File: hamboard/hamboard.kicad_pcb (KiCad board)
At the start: 2 copper layers, 83 parts, among them J1 Conn_01x03_Male, J3 USB_B_Micro, J4 Screw_Terminal_Btn, J5 Screw_Terminal_01x02, J6 programmer, J7 weight, J8 STEPPER, J9 Barrel_Jack, Q1 AO3400A, Q2 S8050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

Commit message: board: bom
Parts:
- added C33: 100nF, Capacitor_SMD:C_0805_2012Metric, F.Cu at (204.5, 92.7)
- added C34: 15pF, Capacitor_SMD:C_0805_2012Metric, F.Cu at (134.6, 90.2)
- added F1: Polyfuse 24V/4A, Fuse:Fuse_2920_7451Metric, F.Cu at (203.2, 111.6)
- added J1: i2c, TerminalBlock:TerminalBlock_bornier-4_P5.08mm, F.Cu at (177.6, 95.7)
- added J10: Conn_01x03_Male, Connector_PinHeader_2.54mm:PinHeader_1x03_P2.54mm_Vertical, F.Cu at (153.9, 82.0)
- added J2: Conn_01x24_Male, Connector_FFC-FPC:Hirose_FH12-24S-0.5SH_1x24-1MP_P0.50mm_Horizontal, F.Cu at (142.0, 83.2)
- added Q2: S8050, Package_TO_SOT_SMD:SOT-23, F.Cu at (176.8, 102.5)
- added Q3: S8050, Package_TO_SOT_SMD:SOT-23, F.Cu at (181.7, 102.5)
- added Q4: MMBT4403, Package_TO_SOT_SMD:SOT-23, F.Cu at (176.8, 110.3)
- added R3: 9k1, Resistor_SMD:R_0805_2012Metric, F.Cu at (134.6, 98.9)
- added R6: 1k, Resistor_SMD:R_0805_2012Metric, F.Cu at (139.1, 90.9)
- added TP10: TestPoint, TestPoint:TestPoint_Pad_D1.5mm, F.Cu at (146.6, 90.4)
- added TP11: TestPoint, TestPoint:TestPoint_Pad_D1.5mm, F.Cu at (143.0, 90.4)
- C10, C13, C14: value 10uF -> 1uF
- C11: value 10uF -> 100nF
- C12: value 10uF -> 10nF
- C19: value 100nF -> 1uF
- C21, C27, C8: value C -> 10nF
- C24, C6: value C -> 1uF
- C26, C7: value C -> 100nF
- C28: footprint Capacitor_SMD:CP_Elec_8x10 -> Capacitor_SMD:CP_Elec_6.3x7.7
- C3, C9: value 0.1uF -> 100nF
- C30: value 470uF/50V -> 680uF/50V; footprint Capacitor_SMD:CP_Elec_16x17.5 -> Capacitor_THT:CP_Radial_D13.0mm_P5.00mm
- C31: value C -> 100n
- C32: footprint Capacitor_SMD:CP_Elec_10x12.5 -> Capacitor_SMD:CP_Elec_10x10.5
- C4: value C -> 1uf
- C5: value ? -> 100nF
- D1, D2: footprint Diode_SMD:D_SOD-923 -> hamboard:Diodes_DFN1006
- D3: value SD24_SOD323 -> SD24_SOD523; footprint Diode_SMD:D_SOD-323 -> Diode_SMD:D_SOD-523
- D4: value D_Zener -> D_Zener 25V
- D5: footprint lib:DIOM6859X262N -> Diode_SMD:D_SMA
- J3: footprint Connector_USB:USB_Micro-B_Molex-105017-0001 -> Connector_USB:USB_Micro-B_GCT_USB3076-30-A
- J4, J5: footprint Connector_Phoenix_MSTB:PhoenixContact_MSTBA_2,5_2-G-5,08_1x02_P5.08mm_Horizontal -> TerminalBlock:TerminalBlock_bornier-2_P5.08mm
- J8: footprint Connector_Phoenix_MSTB:PhoenixContact_MSTBA_2,5_4-G-5,08_1x04_P5.08mm_Horizontal -> TerminalBlock:TerminalBlock_bornier-4_P5.08mm
- R1, R2, R9: value R -> 10k
- R11: value 0R -> 10k
- R19: value R -> 12k
- U3: footprint Package_SO:SOIC-16_3.9x9.9mm_P1.27mm -> Package_SO:SOP-16_3.9x9.9mm_P1.27mm
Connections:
- net Net-(C18-Pad1) renamed /Stepper_driver/5VOUT
- J4 pad 1: /BTN -> Net-(J4-Pad1)
- R12 pad 1: Net-(Q3-Pad1) -> Net-(R12-Pad1)
- R12 pad 2: Net-(Q2-Pad2) -> Net-(R12-Pad2)
- R13 pad 1: Net-(Q2-Pad1) -> Net-(R13-Pad1)
- R13 pad 2: Net-(Q3-Pad2) -> Net-(R13-Pad2)
- U1 pad 12: Net-(TP1-Pad1) -> Net-(U1-Pad12)
- U1 pad 13: Net-(TP2-Pad1) -> Net-(U1-Pad13)
- U1 pad 14: Net-(TP3-Pad1) -> Net-(U1-Pad14)
- U3 pad 13: Net-(Q3-Pad1) -> Net-(R12-Pad1)
- U3 pad 14: Net-(Q2-Pad1) -> Net-(R13-Pad1)
- U5 pad 23: unconnected-(U5-Pad23) -> Net-(R3-Pad2)
- U5 pad 37: unconnected-(U5-Pad37) -> GND
- U7 pad 4: unconnected-(U7-Pad4) -> GND

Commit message: first pcb layout
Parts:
- removed the J1 at (100.0, 89.1)
- removed the Q2 at (123.6, 72.4)
- removed the Q3 at (130.6, 69.4)
- removed TP1, TP2, TP3, TP6: TestPoint, TestPoint:TestPoint_Pad_D1.5mm
- C15: value 22n -> 22nF
- C17: value 470n -> 470nF
- C31: value 100n -> 100nF
- C4: value 1uf -> 1uF
- D4: footprint Capacitor_SMD:CP_Elec_8x10 -> Diode_SMD:D_MiniMELF
- D5: footprint Diode_SMD:D_SMA -> lib:DIOM6859X262N
- J1: footprint TerminalBlock:TerminalBlock_bornier-4_P5.08mm -> Connector_PinHeader_2.54mm:PinHeader_1x04_P2.54mm_Vertical
- J7: footprint Connector_Phoenix_MSTB:PhoenixContact_MSTBA_2,5_4-G-5,08_1x04_P5.08mm_Horizontal -> TerminalBlock:TerminalBlock_bornier-4_P5.08mm
- R14, R15, R16, R17: value 100R -> 100
- moved F1 176.3 mm to (39.3, 46.7)
- moved C33 170.5 mm to (34.0, 89.7), turned to -90 degrees
- moved C17 153.3 mm to (29.2, 86.6), turned to 180 degrees
- moved R18 152.7 mm to (29.2, 84.6)
- moved U5 149.4 mm to (35.1, 84.1), turned to 180 degrees
- moved Q3 142.9 mm to (38.9, 96.8)
- moved C18 139.5 mm to (29.2, 82.5)
- moved J8 138.5 mm to (21.3, 74.2), turned to -90 degrees
- moved Q2 137.9 mm to (38.9, 100.6)
- moved C20 136.2 mm to (36.8, 78.7), turned to 90 degrees
- moved C21 129.8 mm to (38.9, 78.7), turned to 90 degrees
- moved C28 129.7 mm to (30.7, 73.7), turned to 180 degrees
- moved C15 127.5 mm to (29.2, 88.9), turned to 180 degrees
- moved C16 124.9 mm to (32.0, 89.7), turned to -90 degrees
- moved TP10 123.2 mm to (23.9, 101.6)
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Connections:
- J10 pad 1: Net-(U1-Pad14) -> Net-(J10-Pad1)
- J10 pad 2: Net-(U1-Pad13) -> Net-(J10-Pad2)
- J10 pad 3: Net-(U1-Pad12) -> Net-(J10-Pad3)
- J5 pad 1: +24V -> Net-(J5-Pad1)
- J5 pad 2: Net-(J5-Pad2) -> +24V
- Q1 pad 3: Net-(J5-Pad2) -> Net-(J5-Pad1)
- U1 pad 10: /STEPPER_EN -> Net-(J10-Pad3)
- U1 pad 11: /STEPPER_DIR -> Net-(J10-Pad2)
- U1 pad 12: Net-(U1-Pad12) -> Net-(J10-Pad1)
- U1 pad 13: Net-(U1-Pad13) -> /STEPPER_EN
- U1 pad 14: Net-(U1-Pad14) -> /STEPPER_DIR
- U1 pad 6: /CAM_RST -> /CAM_PWN
- U1 pad 7: /CAM_PWN -> /CAM_RST
- U2 pad 10: /CAM_Y2 -> /CAM_Y7
- U2 pad 11: /CAM_Y5 -> /CAM_Y8
- U2 pad 12: /CAM_Y3 -> /CAM_XCLK
- U2 pad 13: /I2C_SDA -> /CAM_Y9
- U2 pad 14: /STEPPER_SCK -> /CAM_HREF
- U2 pad 16: /I2C_SCL -> /CAM_VSYNC
- U2 pad 23: /CAM_Y9 -> /I2C_SCL
- U2 pad 24: /CAM_HREF -> /I2C_SDA
- U2 pad 26: /STEPPER_SDI -> /STEPPER_STEP
- U2 pad 29: /CAM_VSYNC -> /STEPPER_SDO
- U2 pad 30: /CAM_XCLK -> /STEPPER_SDI
- U2 pad 31: /STEPPER_CS -> /STEPPER_SCK
- U2 pad 33: /STEPPER_STEP -> /STEPPER_CS
- U2 pad 36: /CAM_PCLK -> /BTN
- U2 pad 39_1: Net-(U2-Pad39_1) -> GND
- U2 pad 39_2: Net-(U2-Pad39_1) -> GND
- U2 pad 39_3: Net-(U2-Pad39_1) -> GND
- U2 pad 39_4: Net-(U2-Pad39_1) -> GND
- U2 pad 39_5: Net-(U2-Pad39_1) -> GND
- U2 pad 39_6: Net-(U2-Pad39_1) -> GND
- U2 pad 39_7: Net-(U2-Pad39_1) -> GND
- U2 pad 39_8: Net-(U2-Pad39_1) -> GND
- U2 pad 39_9: Net-(U2-Pad39_1) -> GND
- U2 pad 4: /CAM_Y7 -> /CAM_Y4
- U2 pad 5: /CAM_Y6 -> /CAM_Y3
- U2 pad 6: /BTN -> /CAM_Y5
- U2 pad 7: /CAM_Y8 -> /CAM_Y2
- U2 pad 8: /CAM_Y4 -> /CAM_Y6
- U2 pad 9: /STEPPER_SDO -> /CAM_PCLK
- U5 pad 13: Net-(J8-Pad3) -> Net-(J8-Pad2)
- U5 pad 15: Net-(J8-Pad4) -> Net-(J8-Pad1)
- U5 pad 32: Net-(J8-Pad2) -> Net-(J8-Pad3)
- U5 pad 34: Net-(J8-Pad1) -> Net-(J8-Pad4)
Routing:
- net +3V3: track 0.00 -> 258.0 mm, vias 0 -> 2
- net +24V: track 0.00 -> 118.6 mm
- net /IO0: track 0.00 -> 81.4 mm, vias 0 -> 3
- net /I2C_SDA: track 0.00 -> 75.2 mm, vias 0 -> 1
- net /EN: track 0.00 -> 73.9 mm
- net /CAM_PWN: track 0.00 -> 71.4 mm, vias 0 -> 2
- net /I2C_SCL: track 0.00 -> 70.3 mm, vias 0 -> 1
- net /CAM_RST: track 0.00 -> 68.7 mm, vias 0 -> 2
- net /WEIGHT_CLK: track 0.00 -> 53.7 mm, vias 0 -> 2
- net /DBG_TX: track 0.00 -> 37.7 mm
- net /DBG_RX: track 0.00 -> 36.4 mm, vias 0 -> 2
- net /STEPPER_STEP: track 0.00 -> 28.1 mm
- net /STEPPER_EN: track 0.00 -> 27.0 mm, vias 0 -> 2
- net /STEPPER_SDO: track 0.00 -> 26.7 mm
- net /STEPPER_SDI: track 0.00 -> 26.4 mm
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- added copper zone on B.Cu, net GND
- added copper zone on F.Cu, net GND
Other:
- board outline added: 89.7 x 63 mm

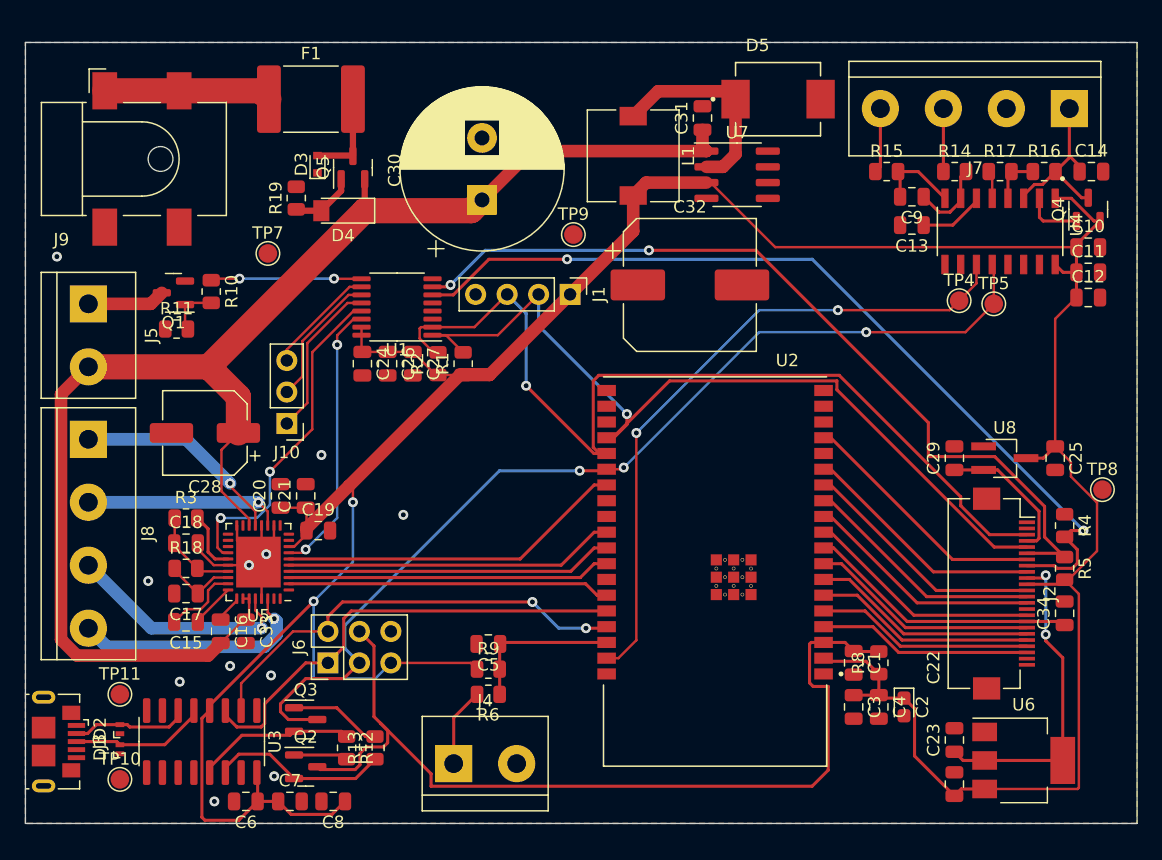
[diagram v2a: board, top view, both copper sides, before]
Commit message: pcb: added screws and rerouted everything
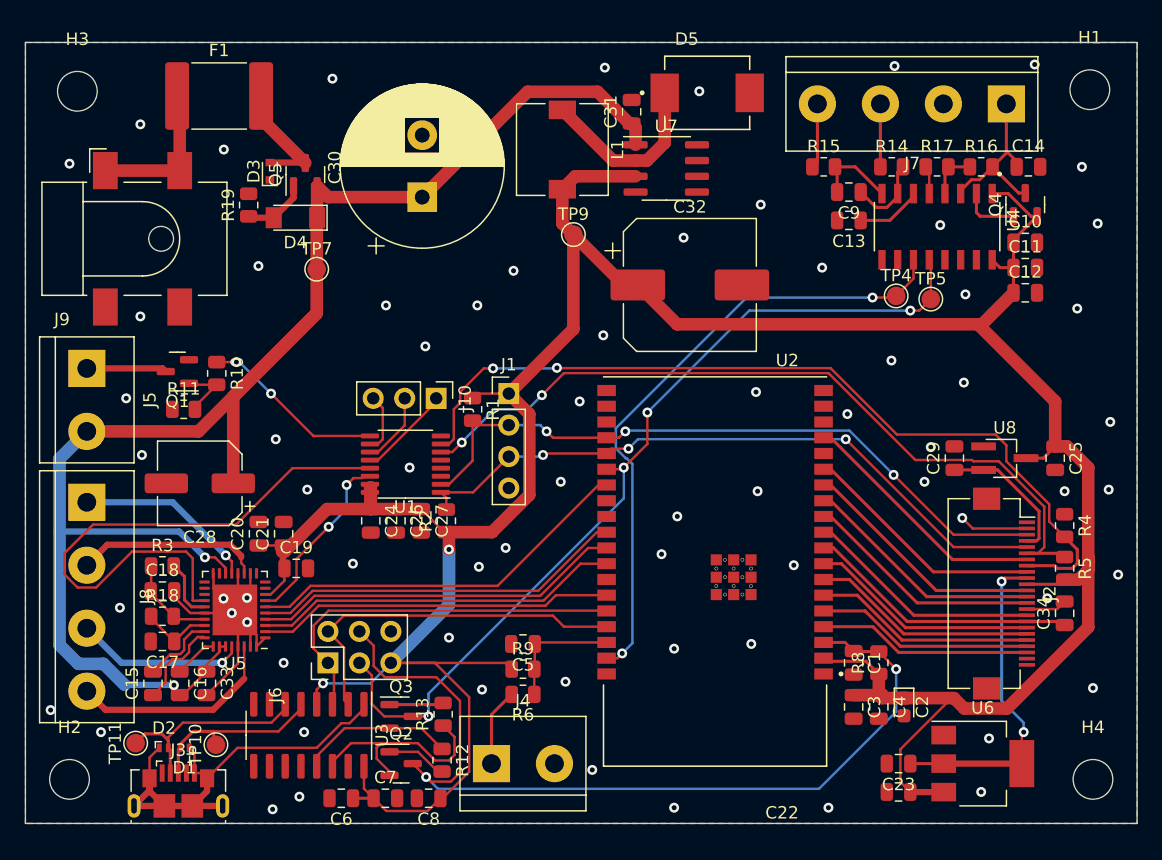
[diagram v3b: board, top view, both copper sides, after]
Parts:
- removed TP8: TestPoint, TestPoint:TestPoint_Pad_D1.5mm
- added H1: MountingHole, MountingHole:MountingHole_3.2mm_M3, F.Cu at (102.1, 46.0)
- added H2: MountingHole, MountingHole:MountingHole_3.2mm_M3, F.Cu at (19.8, 101.6)
- added H3: MountingHole, MountingHole:MountingHole_3.2mm_M3, F.Cu at (20.4, 46.1)
- added H4: MountingHole, MountingHole:MountingHole_3.2mm_M3, F.Cu at (102.4, 101.6)
- moved C24 12.7 mm to (44.1, 80.7)
- moved C26 12.7 mm to (46.1, 80.7)
- moved C27 12.7 mm to (48.2, 80.7)
- moved R2 12.7 mm to (50.2, 80.7)
- moved U1 12.7 mm to (46.9, 76.2)
- moved J10 12.2 mm to (49.4, 70.9), turned to -90 degrees
- moved J3 10.5 mm to (28.6, 102.5), turned to 0 degrees
- moved J1 9.40 mm to (55.2, 70.5), turned to 0 degrees
- moved U3 8.65 mm to (39.1, 98.0)
- moved TP10 8.24 mm to (31.6, 98.8), turned to 90 degrees
- moved R12 7.76 mm to (49.9, 100.1)
- moved C7 7.70 mm to (45.3, 103.1)
- moved C8 7.70 mm to (48.8, 103.1)
- moved C6 7.70 mm to (41.7, 103.1)
- moved Q2 7.70 mm to (46.6, 100.3)
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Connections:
- J1 pad 2: /I2C_SCL -> /I2C_SDA
- J1 pad 3: /I2C_SDA -> /I2C_SCL
- R1 pad 2: /I2C_SCL -> /I2C_SDA
- R2 pad 2: /I2C_SDA -> /I2C_SCL
- U1 pad 6: /CAM_PWN -> /CAM_RST
- U1 pad 7: /CAM_RST -> /CAM_PWN
- U2 pad 23: /I2C_SCL -> /I2C_SDA
- U2 pad 24: /I2C_SDA -> /I2C_SCL
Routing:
- net GND: track 21.5 -> 77.6 mm, vias 11 -> 71
- net /I2C_SDA: track 75.2 -> 55.6 mm, vias 1 -> 3
- net /STEPPER_EN: track 27.0 -> 45.8 mm, vias 2 -> 0
- net /I2C_SCL: track 70.3 -> 54.2 mm, vias 1 -> 3
- net +24V: track 118.6 -> 132.1 mm, vias 0 -> 2
- net /IO0: track 81.4 -> 71.8 mm, vias 3 -> 4
- net /STEPPER_DIR: track 22.3 -> 14.0 mm
- net Net-(D2-Pad2): track 9.48 -> 17.5 mm
- net /DBG_RX: track 36.4 -> 29.9 mm, vias 2 -> 0
- net /DBG_TX: track 37.7 -> 31.2 mm
- net Net-(J10-Pad1): track 12.9 -> 7.58 mm
- net Net-(J10-Pad2): track 10.9 -> 5.88 mm
- net Net-(J8-Pad3): track 18.7 -> 13.7 mm
- net /CAM_RST: track 68.7 -> 63.8 mm
- net Net-(J10-Pad3): track 9.00 -> 4.82 mm
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
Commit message: board: correct DRC issues
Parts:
- removed TP5: TestPoint, TestPoint:TestPoint_Pad_D1.5mm
- added R7: 0R, Resistor_SMD:R_0805_2012Metric, F.Cu at (89.3, 62.6)
- moved TP10 0.63 mm to (31.6, 98.2)
- moved TP11 0.18 mm to (25.0, 98.6)
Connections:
- U2 pad 40: (no net) -> GND
- U2 pad 41: (no net) -> GND
- U2 pad 42: (no net) -> GND
- U2 pad 43: (no net) -> GND
- U2 pad 44: (no net) -> GND
- U2 pad 45: (no net) -> GND
- U2 pad 46: (no net) -> GND
- U2 pad 47: (no net) -> GND
- U2 pad 48: (no net) -> GND
- U2 pad 49: (no net) -> GND
- U2 pad 50: (no net) -> GND
- U2 pad 51: (no net) -> GND
- U4 pad 12: /IO0 -> /WEIGHT_DATA
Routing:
- net /IO0: track 71.8 -> 68.3 mm
- net /WEIGHT_DATA: track 0.00 -> 2.08 mm
- net GND: track 77.6 -> 79.3 mm, vias 71 -> 72
- net Net-(D1-Pad2): track 14.8 -> 13.9 mm

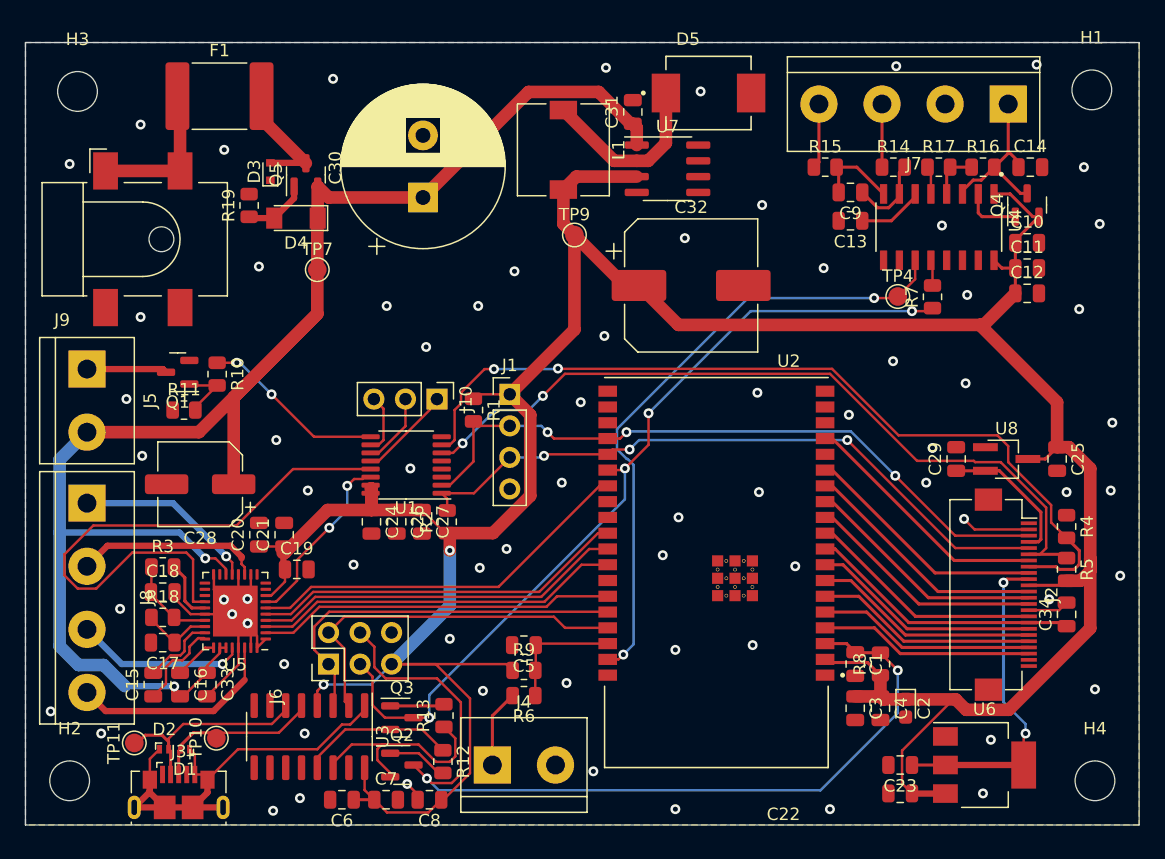
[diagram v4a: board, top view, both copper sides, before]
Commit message: board: fixed esp heat pads
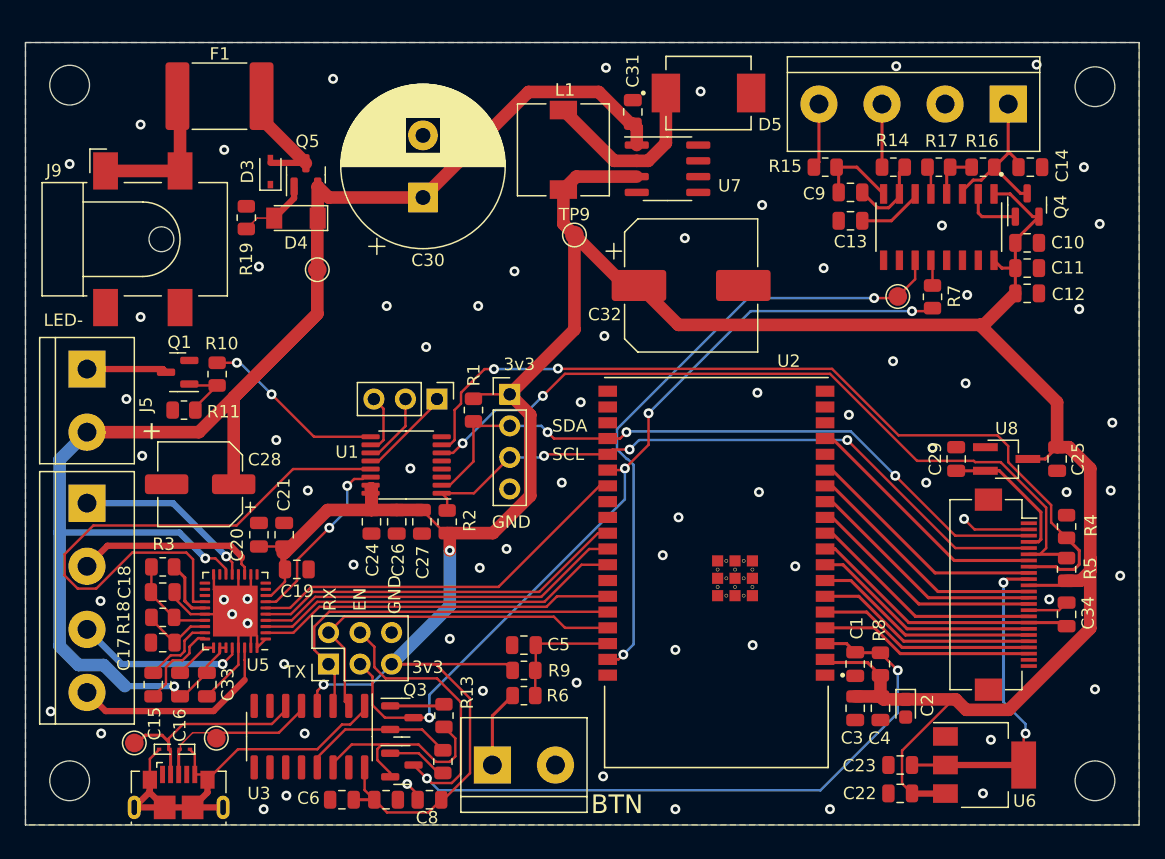
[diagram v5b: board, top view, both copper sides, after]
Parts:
- D1, D2: footprint hamboard:Diodes_DFN1006 -> Diode_SMD:D_SOD-923
- D3: footprint Diode_SMD:D_SOD-523 -> Diode_SMD:D_SOD-323
- TP4: value TestPoint -> W_CLK
- TP7: value TestPoint -> 24V
- U3: footprint Package_SO:SOP-16_3.9x9.9mm_P1.27mm -> Package_SO:SOIC-16_3.9x9.9mm_P1.27mm
- moved R19 1.01 mm to (34.0, 56.3)
- moved H3 0.81 mm to (19.8, 45.6)
- moved H1 0.36 mm to (102.4, 45.7)
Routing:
- net Net-(D4-Pad2): track 5.12 -> 5.81 mm
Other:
- board text added: "+"
- board text added: "3v3"
- board text added: "BTN"
- board text added: "EN"
- board text added: "GND"
- board text added: "LED-"
- board text added: "RX"
- board text added: "SCL"
- board text added: "SDA"
- board text added: "TX"
